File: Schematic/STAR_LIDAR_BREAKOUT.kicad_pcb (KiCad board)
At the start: 2 copper layers, 38.5 x 35.5 mm, 8 parts, among them J1 1028585, J2 TBC05-03-1-G-G, Q1 FDD4141

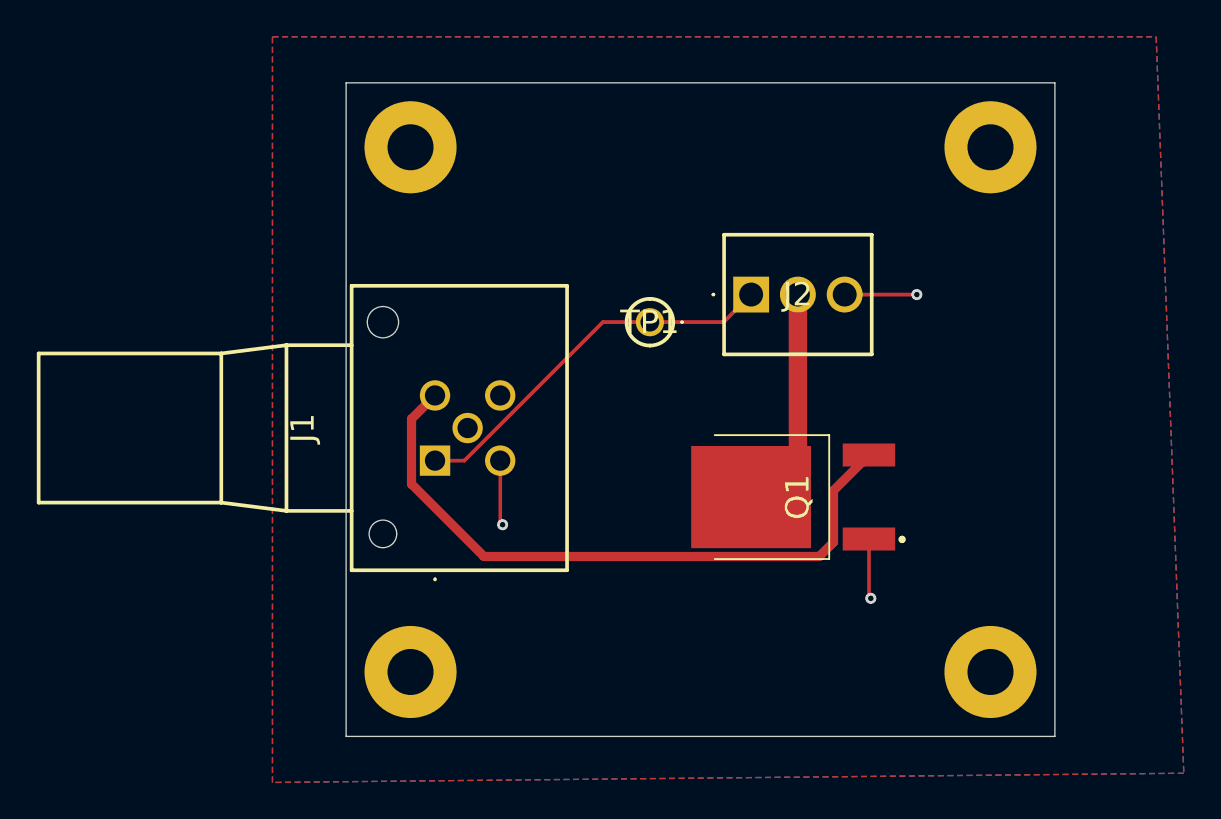
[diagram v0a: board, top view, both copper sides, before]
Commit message: put some cheaper parts
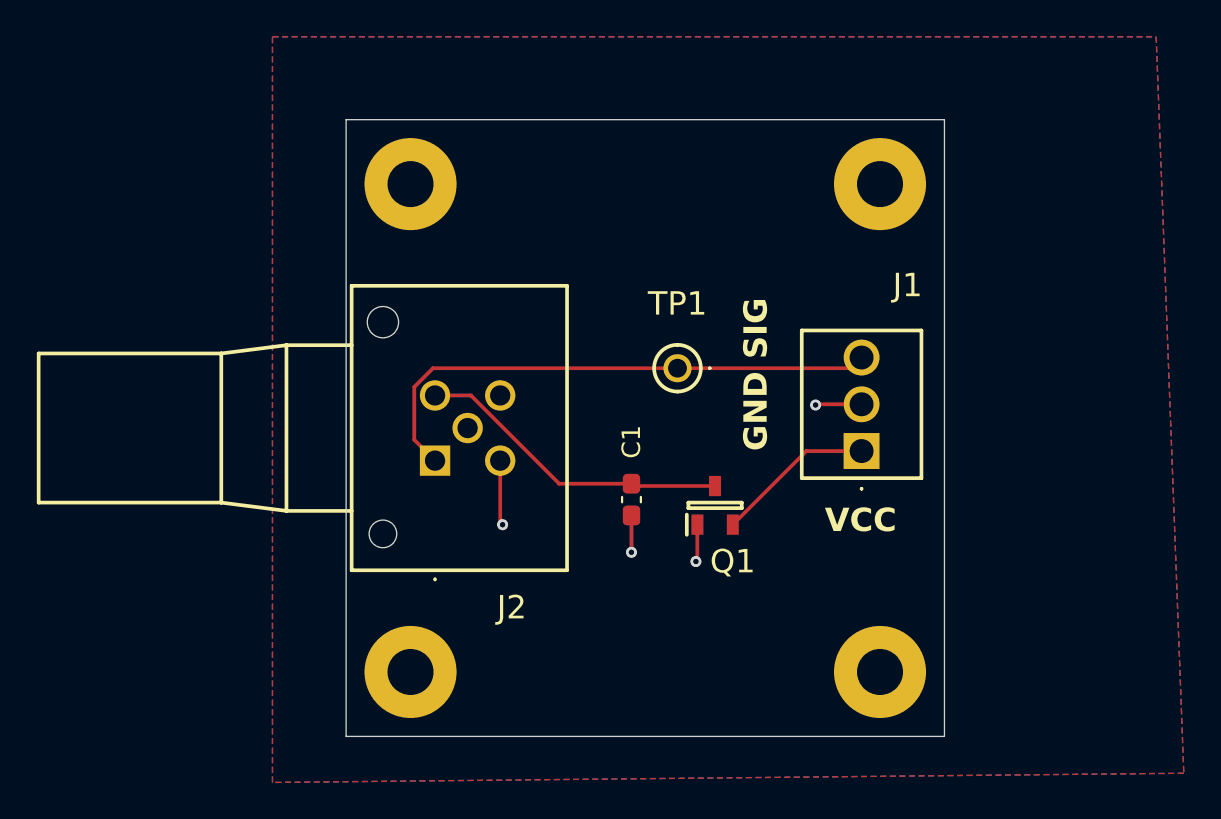
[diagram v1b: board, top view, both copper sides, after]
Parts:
- added C1: 100n, Capacitor_SMD:C_0603_1608Metric_Pad1.08x0.95mm_HandSolder, F.Cu at (155.5, 109.1)
- Q1: value FDD4141 -> ZXMP10A13FTA; footprint FDD4141:FQD1N80TM -> ZXMP10A13FTA:SOT96P240X110-3N
- moved J1 10.4 mm to (168.0, 106.5), turned to 90 degrees
- moved REF** 6.32 mm to (169.0, 92.0)
- moved REF** 6.00 mm to (169.0, 118.5)
- moved TP1 2.92 mm to (158.0, 102.0)
- moved Q1 2.01 mm to (160.0, 109.5)
- moved REF** 2.00 mm to (143.5, 92.0)
- renumbered J2 to J1, J1 to J2
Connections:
- J1 pad 1: /PORT_1_TO_LIDAR_2_SYNC -> Net-(Q1-D)
- J1 pad 2: Net-(Q1-D) -> GND
- J1 pad 3: GND -> /PORT_1_TO_LIDAR_2_SYNC
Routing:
- net /PORT_2_TO_LIDAR_1_VCC: track 35.7 -> 17.2 mm
- net /PORT_1_TO_LIDAR_2_SYNC: track 20.9 -> 29.4 mm
- net Net-(Q1-D): track 12.1 -> 8.66 mm
- net GND: track 10.7 -> 10.1 mm, vias 3 -> 4
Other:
- board size 38.5 x 35.5 mm -> 32.5 x 33.5 mm
- board text added: "GND"
- board text added: "SIG"
- board text added: "VCC"

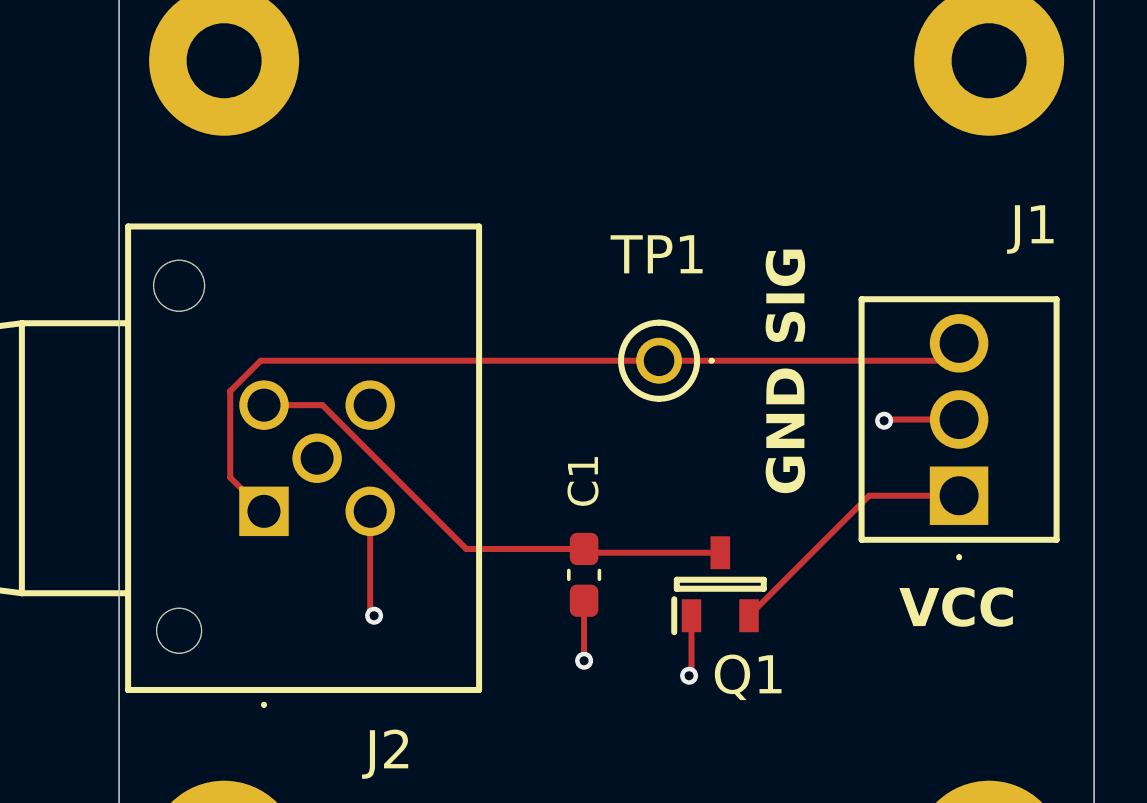
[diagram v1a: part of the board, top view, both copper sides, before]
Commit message: updated lidar breakout board
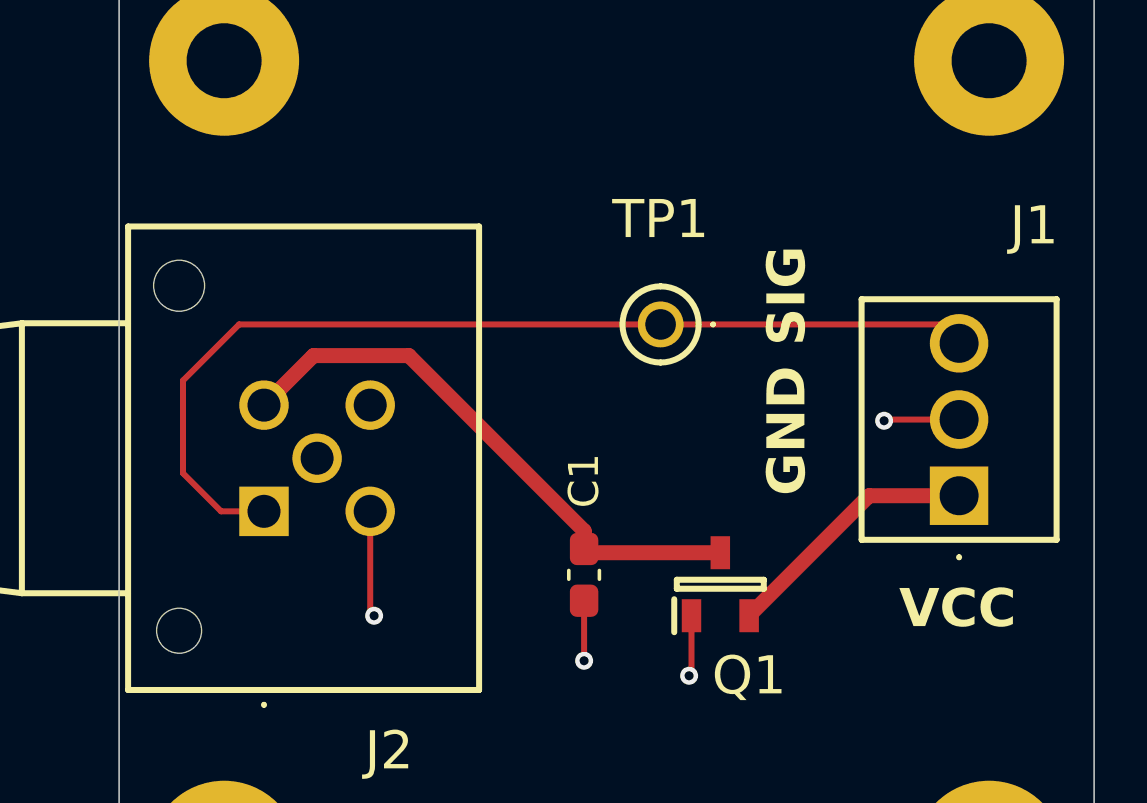
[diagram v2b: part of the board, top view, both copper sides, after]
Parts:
- moved TP1 1.21 mm to (158.1, 100.8)
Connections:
- REF** pad 1: (no net) -> GND (x3)
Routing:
- net /PORT_1_TO_LIDAR_2_SYNC: track 29.4 -> 33.2 mm
- net /PORT_2_TO_LIDAR_1_VCC: track 17.2 -> 19.0 mm
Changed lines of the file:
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@@
 			(outputformat 1)
 			(mirror no)
-			(drillshape 1)
+			(drillshape 0)
 			(scaleselection 1)
-			(outputdirectory "")
+			(outputdirectory "LiDAR Breakout Board Manufacture Items/")
 		)
 	)
@@
 			(layers "*.Cu" "*.Mask")
 			(remove_unused_layers no)
+			(net 3 "GND")
 			(zone_connect 2)
 		)
@@
 			(layers "*.Cu" "*.Mask")
 			(remove_unused_layers no)
+			(net 3 "GND")
 			(zone_connect 2)
 		)
@@
 	(footprint "3825:3825"
 		(layer "F.Cu")
-		(at 158 102)
+		(at 158.05 100.79)
 		(descr "3825-1")
 		(tags "Test Point")
@@
 			(layers "*.Cu" "*.Mask")
 			(remove_unused_layers no)
+			(net 3 "GND")
 			(zone_connect 2)
 		)
@@
 		(start 168 106.5)
 		(end 165 106.5)
-		(width 0.2)
+		(width 0.5)
 		(layer "F.Cu")
 		(net 1)
@@
 		(start 165 106.5)
 		(end 161 110.5)
+		(width 0.5)
+		(layer "F.Cu")
+		(net 1)
+	)
+	(segment
+		(start 167.37 100.79)
+		(end 168 101.42)
 		(width 0.2)
 		(layer "F.Cu")
-		(net 1)
+		(net 2)
 	)
 	(segment
-		(start 143.704 103.013595)
-		(end 143.704 105.894)
+		(start 158.05 100.79)
+		(end 167.37 100.79)
 		(width 0.2)
 		(layer "F.Cu")
@@
 	)
 	(segment
-		(start 143.704 105.894)
+		(start 143.4 107.02)
 		(end 144.83 107.02)
 		(width 0.2)
@@
 	)
 	(segment
-		(start 158 102)
-		(end 144.717595 102)
+		(start 142.13 105.75)
+		(end 143.4 107.02)
 		(width 0.2)
 		(layer "F.Cu")
@@
 	)
 	(segment
-		(start 167.42 102)
-		(end 168 101.42)
+		(start 158.05 100.79)
+		(end 144 100.79)
 		(width 0.2)
 		(layer "F.Cu")
@@
 	)
 	(segment
-		(start 158 102)
-		(end 167.42 102)
+		(start 144 100.79)
+		(end 142.13 102.66)
 		(width 0.2)
 		(layer "F.Cu")
@@
 	)
 	(segment
-		(start 144.717595 102)
-		(end 143.704 103.013595)
+		(start 142.13 102.66)
+		(end 142.13 105.75)
 		(width 0.2)
 		(layer "F.Cu")
@@
 	)
 	(segment
-		(start 144.83 103.48)
-		(end 146.777595 103.48)
-		(width 0.2)
+		(start 155.5 107.67)
+		(end 149.66 101.83)
+		(width 0.5)
 		(layer "F.Cu")
 		(net 4)
@@
 		(start 160.04 108.4)
 		(end 155.625 108.4)
-		(width 0.2)
+		(width 0.5)
 		(layer "F.Cu")
 		(net 4)
 	)
 	(segment
-		(start 151.572595 108.275)
-		(end 155.5 108.275)
-		(width 0.2)
+		(start 155.5 108.275)
+		(end 155.5 107.67)
+		(width 0.5)
 		(layer "F.Cu")
 		(net 4)
 	)
 	(segment
-		(start 146.777595 103.48)
-		(end 151.572595 108.275)
-		(width 0.2)
+		(start 149.66 101.83)
+		(end 146.48 101.83)
+		(width 0.5)
 		(layer "F.Cu")
 		(net 4)
@@
 		(start 155.625 108.4)
 		(end 155.5 108.275)
-		(width 0.2)
+		(width 0.5)
 		(layer "F.Cu")
 		(net 4)
+	)
+	(segment
+		(start 146.48 101.83)
+		(end 144.83 103.48)
+		(width 0.5)
+		(layer "F.Cu")
+		(net 4)
